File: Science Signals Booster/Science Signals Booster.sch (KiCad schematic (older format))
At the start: 7 parts

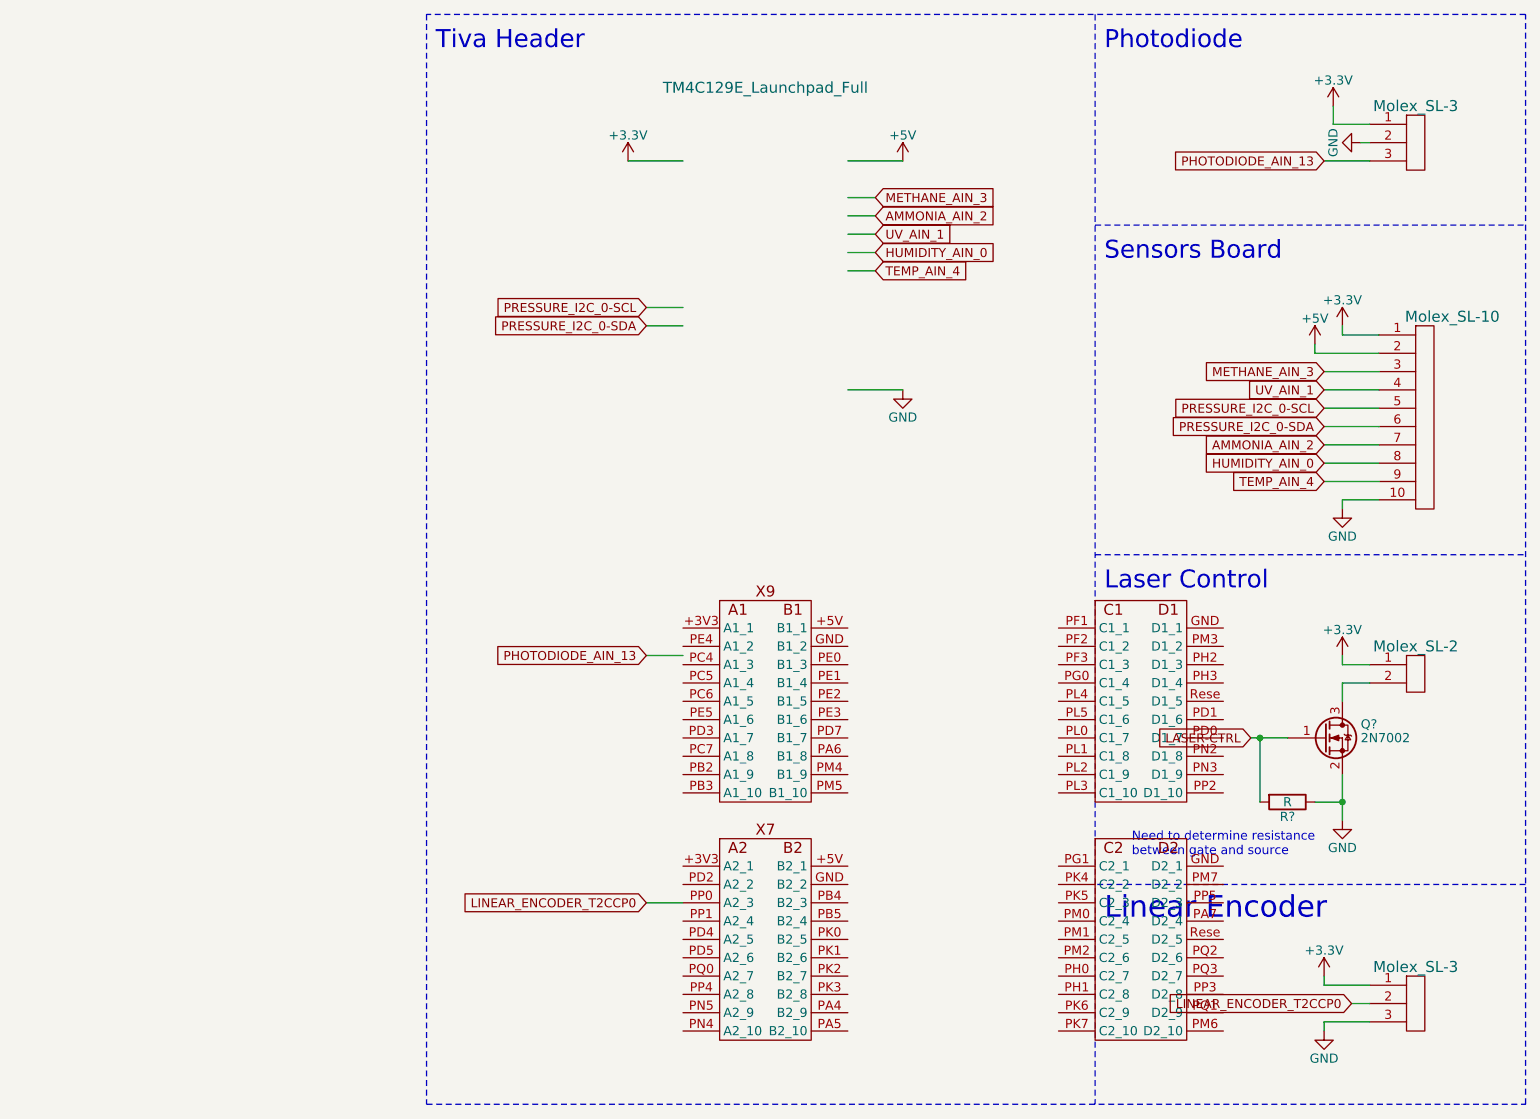
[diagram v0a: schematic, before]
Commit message: Added power and filtering section for andersons, oki, etc.
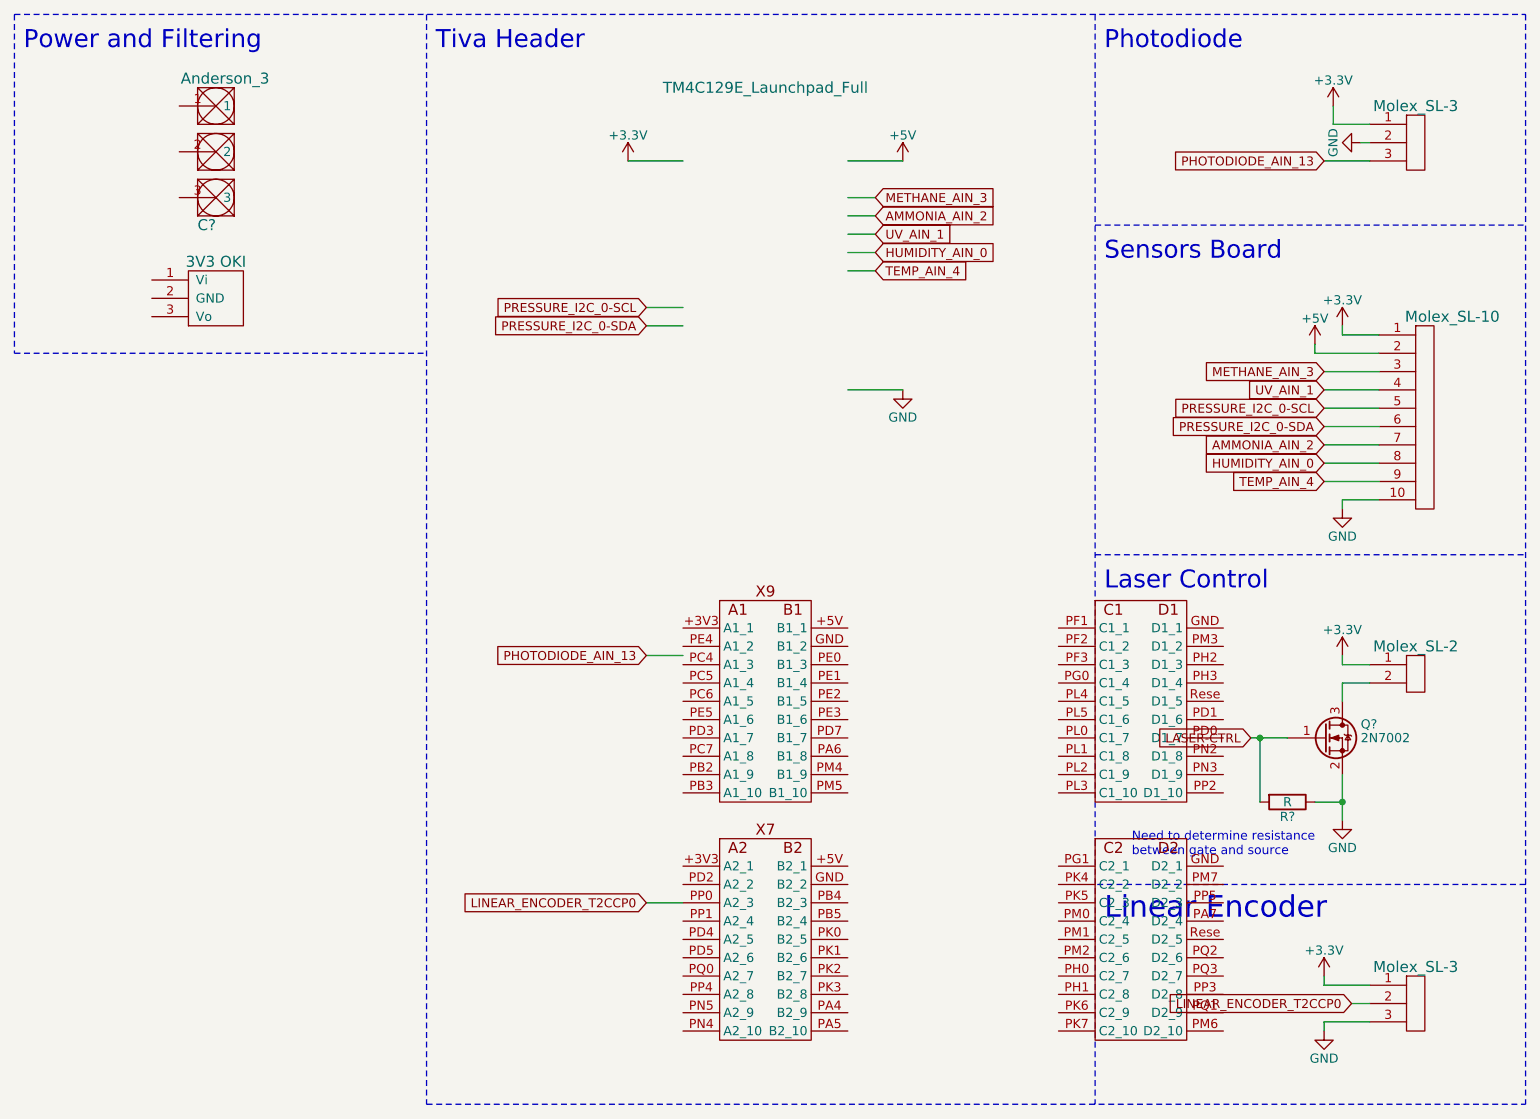
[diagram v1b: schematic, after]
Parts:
- added C?: Anderson_3, symbol Anderson_3
- added U?: 3V3 OKI, symbol OKI
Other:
- note added: "Power and Filtering"
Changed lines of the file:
@@
 LIBS:contrib
 LIBS:valves
-LIBS:MRDT-Actives
-LIBS:MRDT-Connectors
-LIBS:MRDT-Devices
-LIBS:MRDT-Drill_Holes
-LIBS:MRDT-Headers
-LIBS:MRDT-ICs
-LIBS:MRDT-Passives
-LIBS:MRDT-Shields
-LIBS:MRDT-Silkscreens
-LIBS:MRDT-Switches
+LIBS:MRDT_Actives
+LIBS:MRDT_Connectors
+LIBS:MRDT_Devices
+LIBS:MRDT_Drill_Holes
+LIBS:MRDT_Headers
+LIBS:MRDT_ICs
+LIBS:MRDT_Passives
+LIBS:MRDT_Shields
+LIBS:MRDT_Silkscreens
+LIBS:MRDT_Switches
+LIBS:Science Signals Booster-cache
 EELAYER 25 0
 EELAYER END
@@
 	8850 2300 8850 2350
 Wire Notes Line
-	10000 6450 10000 500
+	10000 500  10000 6450
 Wire Wire Line
 	8900 3050 9200 3050
@@
 	9150 1200 9100 1200
 Wire Notes Line
-	10000 500  4000 500
+	1750 500  10000 500
 Wire Notes Line
 	7650 1650 10000 1650
@@
 Wire Wire Line
 	5200 5350 5400 5350
+$Comp
+L OKI U?
+U 1 1 5AB04F9D
+P 2700 2200
+F 0 "U?" H 2550 1950 60  0001 C CNN
+F 1 "3V3 OKI" H 2850 2550 60  0000 C CNN
+F 2 "" H 2450 2100 60  0001 C CNN
+F 3 "" H 2450 2100 60  0001 C CNN
+	1    2700 2200
+	1    0    0    -1
+$EndComp
+$Comp
+L Anderson_3 C?
+U 1 1 5AB04FDB
+P 2750 1600
+F 0 "C?" H 2800 1550 60  0000 C CNN
+F 1 "Anderson_3" H 2900 2350 60  0000 C CNN
+F 2 "" H 2800 1050 60  0001 C CNN
+F 3 "" H 2800 1050 60  0001 C CNN
+	1    2750 1600
+	1    0    0    -1
+$EndComp
+Text Notes 1800 700  0    98   ~ 0
+Power and Filtering
+Wire Notes Line
+	1750 500  1750 2350
+Wire Notes Line
+	1750 2350 4000 2350
 $EndSCHEMATC

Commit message: Added notes from meeting about changes needed for signals board schematic
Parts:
- U?: value 3V3 OKI -> 5V OKI
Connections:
- net labels added: PVDD
- wire segments 42 -> 46
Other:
- note added: "2 5v okis"
- note added: "Add sections from the eagle board,\nuse 3v3 from the tiva after giving it 5v,\nno sensor conditioning (from eagle board),\nadd Mag inputs for linear encoder"
- note added: "Connect all GNDs"
- note added: "Contact Nicole and Rausch about flap \nand carosal labels in eagle schematic for last\nyears board\n(we think we don't need them)"
- note added: "Laser Control (recreate using circuit from last years board)"
- note added: "Power"
- note removed: "Laser Control"
- note removed: "Need to determine resistance \nbetween gate and source"
- note removed: "Power and Filtering"
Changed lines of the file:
@@
 $EndDescr
 Text Notes 7700 3650 0    98   ~ 0
-Laser Control
+Laser Control (recreate using circuit from last years board)
 $Comp
 L +3.3V #PWR?
@@
 	0    1    1    0
 $EndComp
-Text Notes 7850 5100 0    49   ~ 0
-Need to determine resistance \nbetween gate and source
 $Comp
 L Molex_SL-10 U?
@@
 P 2700 2200
 F 0 "U?" H 2550 1950 60  0001 C CNN
-F 1 "3V3 OKI" H 2850 2550 60  0000 C CNN
+F 1 "5V OKI" H 2850 2550 60  0000 C CNN
 F 2 "" H 2450 2100 60  0001 C CNN
 F 3 "" H 2450 2100 60  0001 C CNN
@@
 $EndComp
 Text Notes 1800 700  0    98   ~ 0
-Power and Filtering
+Power
 Wire Notes Line
 	1750 500  1750 2350
 Wire Notes Line
 	1750 2350 4000 2350
+$Comp
+L GND #PWR?
+U 1 1 5AB05B69
+P 2300 2100
+F 0 "#PWR?" H 2300 1850 50  0001 C CNN
+F 1 "GND" H 2300 1950 50  0000 C CNN
+F 2 "" H 2300 2100 50  0001 C CNN
+F 3 "" H 2300 2100 50  0001 C CNN
+	1    2300 2100
+	1    0    0    -1
+$EndComp
+Wire Wire Line
+	2300 2100 2300 2050
+Wire Wire Line
+	2300 2050 2500 2050
+Text GLabel 2400 1250 0    49   Input ~ 0
+PVDD
+Text Notes 6100 3650 0    49   ~ 0
+Connect all GNDs
+Text Notes 2000 2750 0    49   ~ 0
+Contact Nicole and Rausch about flap \nand carosal labels in eagle schematic for last\nyears board\n(we think we don't need them)
+Wire Wire Line
+	2400 1250 2650 1250
+Text Notes 1900 1750 0    49   ~ 0
+2 5v okis
+Text Notes 2300 3850 0    49   ~ 0
+Add sections from the eagle board,\nuse 3v3 from the tiva after giving it 5v,\nno sensor conditioning (from eagle board),\nadd Mag inputs for linear encoder
+Text GLabel 2400 1000 0    49   Input ~ 0
+PVDD
+Wire Wire Line
+	2400 1000 2650 1000
 $EndSCHEMATC

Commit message: Added Power section with Oki and Anderson connections
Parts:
- added C? (x2): 10uF, symbol CP
- added C? (x2): 22uF, symbol CP
- added PWR: LED, symbol LED
- added R?: 1k, symbol R
- added U?: 5V OKI, symbol OKI
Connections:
- net labels added: ACT-12V, ACT-5V, LOGIC-12V, LOGIC-5V
- net labels removed: PVDD
- wire segments 46 -> 62
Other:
- note removed: "2 5v okis"
- moved on the sheet: C?
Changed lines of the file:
@@
 	9150 1200 9100 1200
 Wire Notes Line
-	1750 500  10000 500
+	600  500  10000 500
 Wire Notes Line
 	7650 1650 10000 1650
@@
 L OKI U?
 U 1 1 5AB04F9D
-P 2700 2200
-F 0 "U?" H 2550 1950 60  0001 C CNN
-F 1 "5V OKI" H 2850 2550 60  0000 C CNN
-F 2 "" H 2450 2100 60  0001 C CNN
-F 3 "" H 2450 2100 60  0001 C CNN
-	1    2700 2200
+P 1950 2200
+F 0 "U?" H 1800 1950 60  0001 C CNN
+F 1 "5V OKI" H 2100 2550 60  0000 C CNN
+F 2 "" H 1700 2100 60  0001 C CNN
+F 3 "" H 1700 2100 60  0001 C CNN
+	1    1950 2200
 	1    0    0    -1
 $EndComp
@@
 L Anderson_3 C?
 U 1 1 5AB04FDB
-P 2750 1600
-F 0 "C?" H 2800 1550 60  0000 C CNN
-F 1 "Anderson_3" H 2900 2350 60  0000 C CNN
-F 2 "" H 2800 1050 60  0001 C CNN
-F 3 "" H 2800 1050 60  0001 C CNN
-	1    2750 1600
-	1    0    0    -1
-$EndComp
-Text Notes 1800 700  0    98   ~ 0
+P 2200 1400
+F 0 "C?" H 2250 1350 60  0000 C CNN
+F 1 "Anderson_3" H 2350 2150 60  0000 C CNN
+F 2 "" H 2250 850 60  0001 C CNN
+F 3 "" H 2250 850 60  0001 C CNN
+	1    2200 1400
+	1    0    0    -1
+$EndComp
+Text Notes 650  700  0    98   ~ 0
 Power
-Wire Notes Line
-	1750 500  1750 2350
-Wire Notes Line
-	1750 2350 4000 2350
 $Comp
 L GND #PWR?
 U 1 1 5AB05B69
-P 2300 2100
-F 0 "#PWR?" H 2300 1850 50  0001 C CNN
-F 1 "GND" H 2300 1950 50  0000 C CNN
-F 2 "" H 2300 2100 50  0001 C CNN
-F 3 "" H 2300 2100 50  0001 C CNN
-	1    2300 2100
-	1    0    0    -1
-$EndComp
-Wire Wire Line
-	2300 2100 2300 2050
-Wire Wire Line
-	2300 2050 2500 2050
-Text GLabel 2400 1250 0    49   Input ~ 0
-PVDD
+P 1100 2100
+F 0 "#PWR?" H 1100 1850 50  0001 C CNN
+F 1 "GND" H 1100 1950 50  0000 C CNN
+F 2 "" H 1100 2100 50  0001 C CNN
+F 3 "" H 1100 2100 50  0001 C CNN
+	1    1100 2100
+	1    0    0    -1
+$EndComp
+Text GLabel 1850 1050 0    49   Input ~ 0
+LOGIC-12V
 Text Notes 6100 3650 0    49   ~ 0
 Connect all GNDs
-Text Notes 2000 2750 0    49   ~ 0
+Text Notes -1450 2200 0    49   ~ 0
 Contact Nicole and Rausch about flap \nand carosal labels in eagle schematic for last\nyears board\n(we think we don't need them)
 Wire Wire Line
-	2400 1250 2650 1250
-Text Notes 1900 1750 0    49   ~ 0
-2 5v okis
-Text Notes 2300 3850 0    49   ~ 0
+	1850 1050 2100 1050
+Text Notes 2050 4000 0    49   ~ 0
 Add sections from the eagle board,\nuse 3v3 from the tiva after giving it 5v,\nno sensor conditioning (from eagle board),\nadd Mag inputs for linear encoder
-Text GLabel 2400 1000 0    49   Input ~ 0
-PVDD
-Wire Wire Line
-	2400 1000 2650 1000
+Text GLabel 1850 800  0    49   Input ~ 0
+ACT-12V
+Wire Wire Line
+	1850 800  2100 800
+$Comp
+L GND #PWR?
+U 1 1 5AB1C63A
+P 2000 1350
+F 0 "#PWR?" H 2000 1100 50  0001 C CNN
+F 1 "GND" H 2000 1200 50  0000 C CNN
+F 2 "" H 2000 1350 50  0001 C CNN
+F 3 "" H 2000 1350 50  0001 C CNN
+	1    2000 1350
+	1    0    0    -1
+$EndComp
+Wire Wire Line
+	2000 1350 2000 1300
+Wire Wire Line
+	2000 1300 2100 1300
+Text GLabel 1250 1700 0    49   Input ~ 0
+LOGIC-12V
+$Comp
+L CP C?
+U 1 1 5AB1C78D
+P 1400 1850
+F 0 "C?" H 1425 1950 50  0000 L CNN
+F 1 "10uF" H 1425 1750 50  0000 L CNN
+F 2 "" H 1438 1700 50  0001 C CNN
+F 3 "" H 1400 1850 50  0001 C CNN
+	1    1400 1850
+	1    0    0    -1
+$EndComp
+Connection ~ 1400 1700
+Wire Wire Line
+	1100 2050 1100 2100
+Wire Wire Line
+	1750 1700 1750 1950
+$Comp
+L CP C?
+U 1 1 5AB1CD8C
+P 1400 2250
+F 0 "C?" H 1425 2350 50  0000 L CNN
+F 1 "22uF" H 1425 2150 50  0000 L CNN
+F 2 "" H 1438 2100 50  0001 C CNN
+F 3 "" H 1400 2250 50  0001 C CNN
+	1    1400 2250
+	-1   0    0    1
+$EndComp
+Wire Wire Line
+	1250 1700 1750 1700
+Wire Wire Line
+	1400 2000 1400 2100
+Wire Wire Line
+	1100 2050 1750 2050
+Connection ~ 1400 2050
+Wire Wire Line
+	1250 2400 1750 2400
+Wire Wire Line
+	1750 2150 1750 2700
+Text GLabel 1250 2400 0    49   Input ~ 0
+LOGIC-5V
+Connection ~ 1400 2400
+$Comp
+L R R?
+U 1 1 5AB1D544
+P 1600 2700
+F 0 "R?" V 1680 2700 50  0000 C CNN
+F 1 "1k" V 1600 2700 50  0000 C CNN
+F 2 "" V 1530 2700 50  0001 C CNN
+F 3 "" H 1600 2700 50  0001 C CNN
+	1    1600 2700
+	0    -1   -1   0
+$EndComp
+$Comp
+L GND #PWR?
+U 1 1 5AB1D58B
+P 1100 2800
+F 0 "#PWR?" H 1100 2550 50  0001 C CNN
+F 1 "GND" H 1100 2650 50  0000 C CNN
+F 2 "" H 1100 2800 50  0001 C CNN
+F 3 "" H 1100 2800 50  0001 C CNN
+	1    1100 2800
+	1    0    0    -1
+$EndComp
+$Comp
+L LED PWR
+U 1 1 5AB1D5E0
+P 1300 2700
+F 0 "PWR" H 1300 2800 50  0000 C CNN
+F 1 "LED" H 1300 2600 50  0000 C CNN
+F 2 "" H 1300 2700 50  0001 C CNN
+F 3 "" H 1300 2700 50  0001 C CNN
+	1    1300 2700
+	1    0    0    -1
+$EndComp
+Wire Wire Line
+	1150 2700 1100 2700
+Wire Wire Line
+	1100 2700 1100 2800
+Connection ~ 1750 2400
+$Comp
+L OKI U?
+U 1 1 5AB1DAC9
+P 3500 2200
+F 0 "U?" H 3350 1950 60  0001 C CNN
+F 1 "5V OKI" H 3650 2550 60  0000 C CNN
+F 2 "" H 3250 2100 60  0001 C CNN
+F 3 "" H 3250 2100 60  0001 C CNN
+	1    3500 2200
+	1    0    0    -1
+$EndComp
+$Comp
+L GND #PWR?
+U 1 1 5AB1DACF
+P 2650 2100
+F 0 "#PWR?" H 2650 1850 50  0001 C CNN
+F 1 "GND" H 2650 1950 50  0000 C CNN
+F 2 "" H 2650 2100 50  0001 C CNN
+F 3 "" H 2650 2100 50  0001 C CNN
+	1    2650 2100
+	1    0    0    -1
+$EndComp
+Text GLabel 2800 1700 0    49   Input ~ 0
+ACT-12V
+$Comp
+L CP C?
+U 1 1 5AB1DAD6
+P 2950 1850
+F 0 "C?" H 2975 1950 50  0000 L CNN
+F 1 "10uF" H 2975 1750 50  0000 L CNN
+F 2 "" H 2988 1700 50  0001 C CNN
+F 3 "" H 2950 1850 50  0001 C CNN
+	1    2950 1850
+	1    0    0    -1
+$EndComp
+Connection ~ 2950 1700
+Wire Wire Line
+	2650 2050 2650 2100
+Wire Wire Line
+	3300 1700 3300 1950
+$Comp
+L CP C?
+U 1 1 5AB1DADF
+P 2950 2250
+F 0 "C?" H 2975 2350 50  0000 L CNN
+F 1 "22uF" H 2975 2150 50  0000 L CNN
+F 2 "" H 2988 2100 50  0001 C CNN
+F 3 "" H 2950 2250 50  0001 C CNN
+	1    2950 2250
+	-1   0    0    1
+$EndComp
+Wire Wire Line
+	2800 1700 3300 1700
+Wire Wire Line
+	2950 2000 2950 2100
+Wire Wire Line
+	2650 2050 3300 2050
+Connection ~ 2950 2050
+Wire Wire Line
+	2800 2400 3300 2400
+Text GLabel 2800 2400 0    49   Input ~ 0
+ACT-5V
+Connection ~ 2950 2400
+Wire Wire Line
+	3300 2400 3300 2150
+Wire Notes Line
+	600  500  600  3150
+Wire Notes Line
+	600  3150 4000 3150
 $EndSCHEMATC

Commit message: Added photodiodes circuitry and connectors
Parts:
- removed U?: Molex_SL-3, symbol Molex_SL-3
- added C? (x2): 1uF, symbol CP
- added C? (x2): 2.7pF, symbol CP
- added C? (x2): 0.1uF, symbol CP
- added R? (x2): 13.7k, symbol R
- added R? (x2): 280, symbol R
- added R? (x2): 32.3k, symbol R
- added R? (x2): 49.9, symbol R
- added U? (x2): OPA320, symbol OPA333xxDBV
- added U? (x2): Molex_SL-2, symbol Molex_SL-2
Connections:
- net labels added: PHOTODIODE_AIN_12
- wire segments 62 -> 113
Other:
- note removed: "Connect all GNDs"
- moved on the sheet: C?, PWR, Q?, R?

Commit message: Added Laster Control
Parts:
- removed Q?: 2N7002, TO_SOT_Packages_SMD:SOT-23, symbol 2N7002
- removed R?: R, symbol R
- removed U?: Molex_SL-2, symbol Molex_SL-2
- added C?: 33uF, symbol CP
- added C?: 22uF, symbol CP
- added R?: 10k, symbol R
- added R?: 3.92k, symbol R
- added R?: 5k, symbol R
- added U?: BA00DD0WHFP, symbol BA00DD0WHFP
- added U?: Molex_SL_2, symbol Molex_SL_2
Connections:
- net labels added: LASER-CTRl
- net labels removed: LASER-CTRL
- wire segments 113 -> 122
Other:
- note added: "Laser Control"
- note removed: "Laser Control (recreate using circuit from last years board)"

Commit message: Added Spectrometer motor, notes about tiva pin mappings needed. Created device / package associations and generated netlist
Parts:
- removed U?: Molex_SL-3, symbol Molex_SL-3
- added C14: 1uF, Capacitors_SMD:C_0805_HandSoldering, symbol CP
- added U10: LB1930MC, symbol LB1930MC
- added U13: Molex_SL_5, MRDT_Connectors.pretty:MOLEX_SL_5, symbol Molex_SL_5
- added U9: Molex_SL_2, MRDT_Connectors.pretty:MOLEX_SL_2, symbol Molex_SL_2
- C3, C4, C5, C6, C8, C9: renamed from C?; footprint (none) -> Capacitors_SMD:C_0805_HandSoldering
- C7: renamed from C?; footprint (none) -> MRDT_Connectors.pretty:Anderson_3_Horisontal_Side_by_Side
- R1, R10, R11, R12, R2, R3, R4, R5, R6, R7, R8, R9: renamed from R?; footprint (none) -> Resistors_SMD:R_0805_HandSoldering
- U1, U12, U2: renamed from U?; footprint (none) -> MRDT_Connectors.pretty:MOLEX_SL_2
- U11: renamed from U?; footprint (none) -> MRDT_Connectors.pretty:MOLEX_SL_10
- U3, U6: renamed from U?; footprint (none) -> MRDT_Devices.pretty:OKI_Horisontal
- U4, U5: renamed from U?; footprint (none) -> TO_SOT_Packages_SMD:SOT-23-5_HandSoldering
- U7: renamed from U?; footprint (none) -> MRDT_Shields.pretty:TM4C129E_Launchpad_FULL_Booster
- gave numbers to parts that had none: 7
- renumbered PWR to PWR1
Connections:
- net labels added: LASER-CTRL_AIN_7, MOTOR_IN1, MOTOR_IN2, magDECn, magINCn
- net labels removed: LASER-CTRl
- wire segments 122 -> 139
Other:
- note added: "Need TIVA pins selected for IN1, IN2"
- note added: "Need TIVA pins selected for magINC, magDEC"
- note added: "Spectrometer Motor"
- note removed: "Add sections from the eagle board,\nuse 3v3 from the tiva after giving it 5v,\nno sensor conditioning (from eagle board),\nadd Mag inputs for linear encoder"
- note removed: "Contact Nicole and Rausch about flap \nand carosal labels in eagle schematic for last\nyears board\n(we think we don't need them)"
- moved on the sheet: C7, PWR1, R1, R10, R11, R12, R2, R3, R4, R5, R6, R7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
